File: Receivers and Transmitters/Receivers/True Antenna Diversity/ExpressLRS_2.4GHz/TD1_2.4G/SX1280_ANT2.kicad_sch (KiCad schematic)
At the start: 8 parts, among them U3 SX1280IMLTRT, Y2 52MHz

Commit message: Updated schematics for TD1_2.4G receiver: ESP32, SX1280, and RFX2401C blocks
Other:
- company: https://github.com/Paschalis | TeodoraMiu -> https://github.com/Paschalis
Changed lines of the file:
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@@
 		(date "2025-02-23")
 		(rev "1.0")
-		(company "https://github.com/Paschalis | TeodoraMiu")
+		(company "https://github.com/Paschalis")
 		(comment 2 "capabilities in LoRa communication, making it ideal for reliable telemetry.")
 		(comment 3 "The SX1280 is used for its long-range, low-power, and high-performance ")

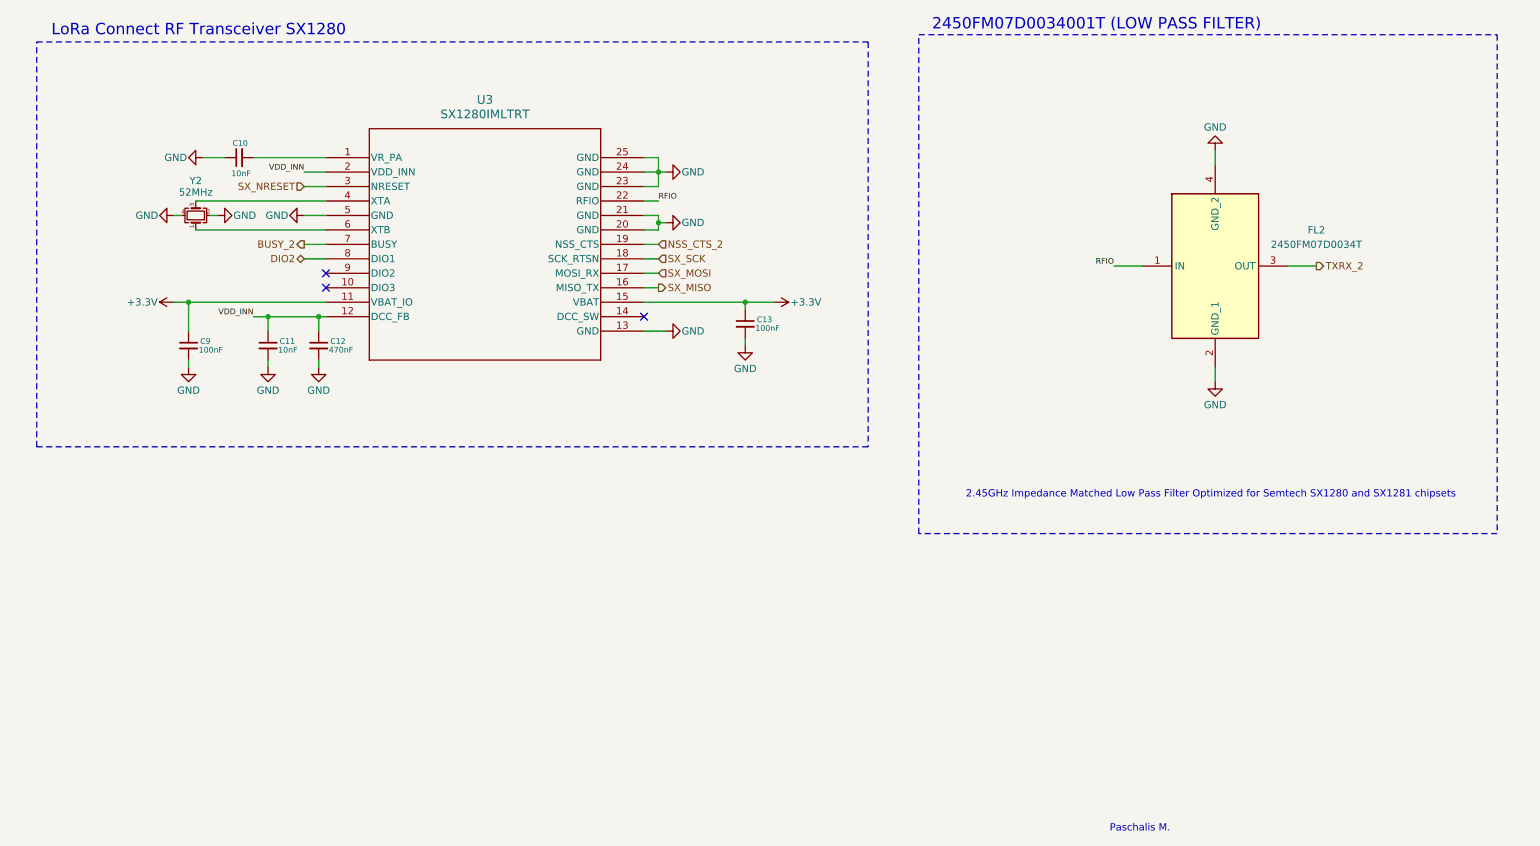
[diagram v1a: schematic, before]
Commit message: Update TD1_2.4G: schematic and PCB revisions, BOM export, README; remove old PCBWay production files
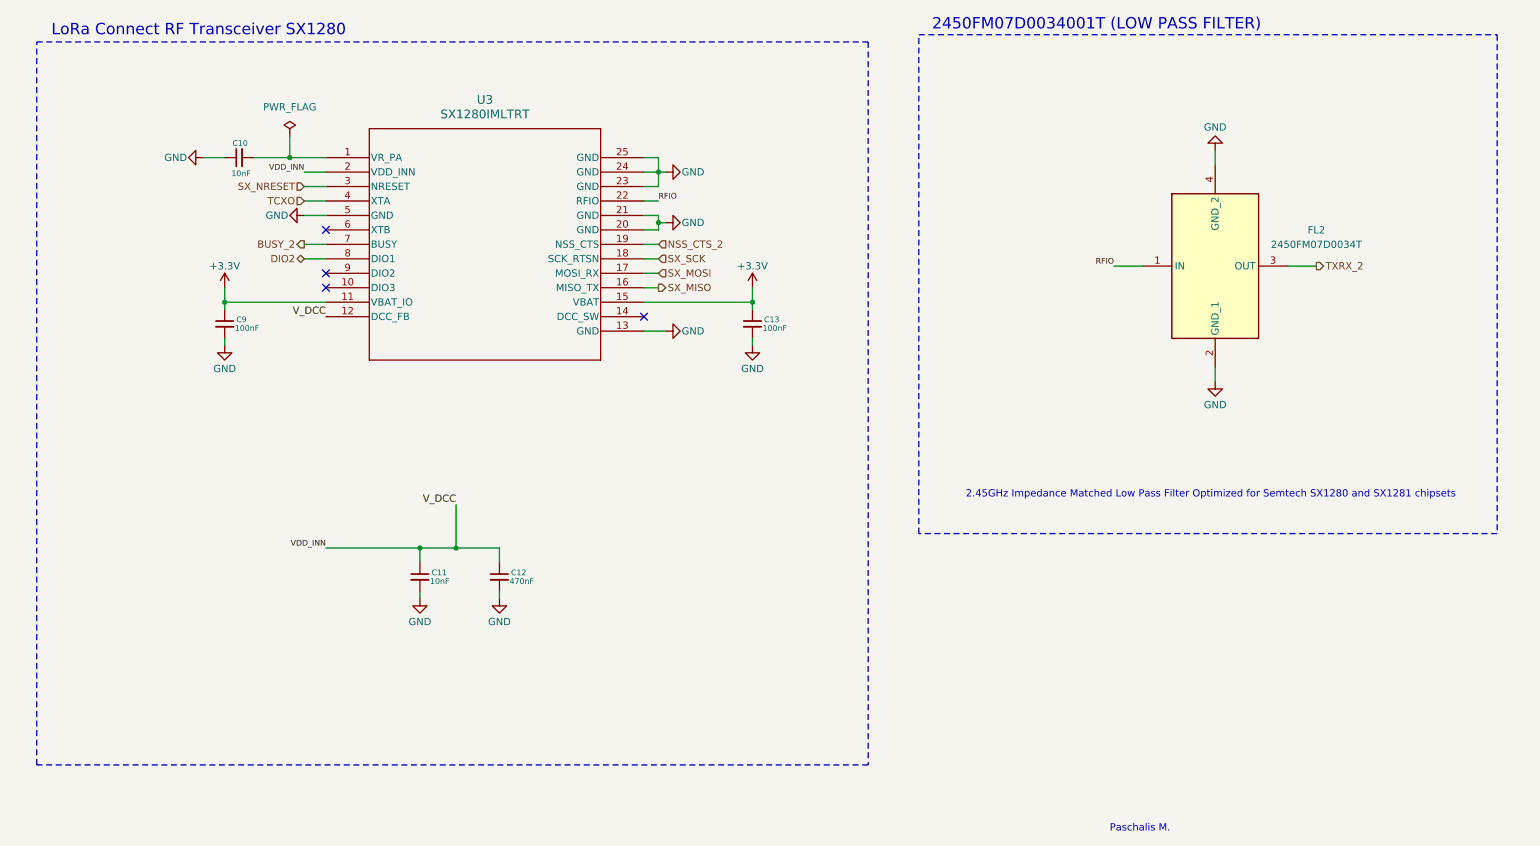
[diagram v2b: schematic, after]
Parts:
- removed Y2: 52MHz, Crystal:Crystal_SMD_2016-4Pin_2.0x1.6mm, symbol Device:Crystal_GND24_Small
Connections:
- net TCXO: now reaches U3.4 (XTA)
- no-connect marks 3 -> 4
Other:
- moved on the sheet: C11, C12, C13, C9
